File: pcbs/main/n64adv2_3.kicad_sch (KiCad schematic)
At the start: 27 parts, among them U12 TLV70218DBVT, U13 TLV70033

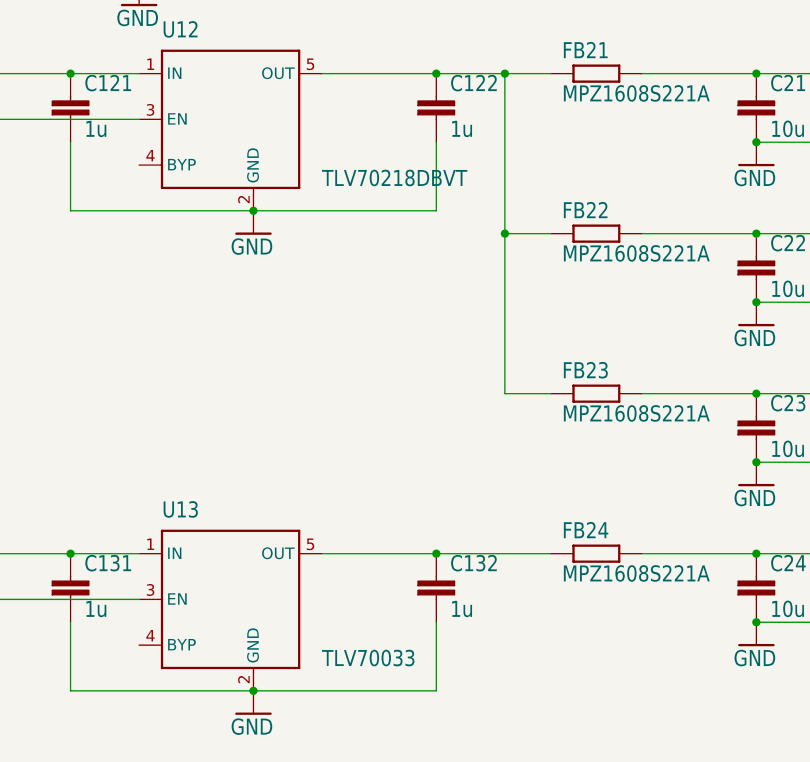
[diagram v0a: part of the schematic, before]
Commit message: update main PCB with minor changes, e.g. ensure that solder mask bridges between 0.5mm pitched pads has min. 0.1mm thickness
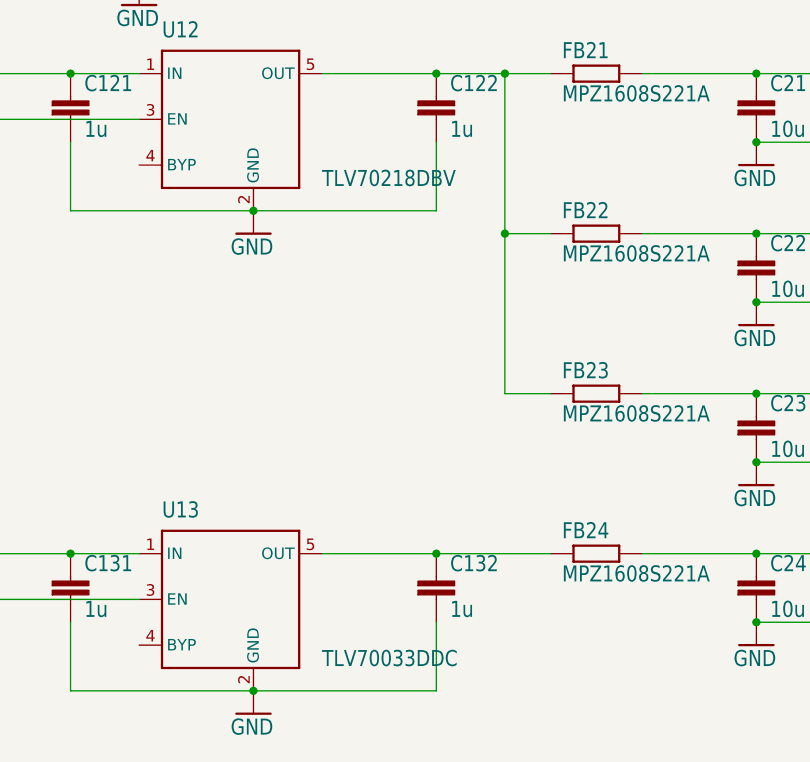
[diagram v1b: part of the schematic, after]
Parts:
- P_5V_IN0, P_GND_2: value (none) -> SMD2; footprint (none) -> n64adv2:SMD1,27-2,54
- U12: value TLV70218DBVT -> TLV70218DBV
- U13: value TLV70033 -> TLV70033DDC
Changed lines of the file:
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@@
       (effects (font (size 1.778 1.5113)) (justify left bottom))
     )
-    (property "Value" "" (id 1) (at 65.278 57.277 0)
+    (property "Value" "SMD2" (id 1) (at 65.278 57.277 0)
       (effects (font (size 1.778 1.5113)) (justify left bottom) hide)
     )
-    (property "Footprint" "" (id 2) (at 68.58 58.42 0)
+    (property "Footprint" "n64adv2:SMD1,27-2,54" (id 2) (at 68.58 58.42 0)
       (effects (font (size 1.27 1.27)) hide)
     )
@@
       (effects (font (size 1.778 1.5113)) (justify left bottom))
     )
-    (property "Value" "TLV70218DBVT" (id 1) (at 127 96.52 0)
+    (property "Value" "TLV70218DBV" (id 1) (at 127 96.52 0)
       (effects (font (size 1.778 1.5113)) (justify left bottom))
     )
@@
       (effects (font (size 1.778 1.5113)) (justify left bottom))
     )
-    (property "Value" "" (id 1) (at 71.882 74.803 0)
+    (property "Value" "SMD2" (id 1) (at 71.882 74.803 0)
       (effects (font (size 1.778 1.5113)) (justify left bottom) hide)
     )
-    (property "Footprint" "" (id 2) (at 68.58 73.66 0)
+    (property "Footprint" "n64adv2:SMD1,27-2,54" (id 2) (at 68.58 73.66 0)
       (effects (font (size 1.27 1.27)) hide)
     )
@@
       (effects (font (size 1.778 1.5113)) (justify left bottom))
     )
-    (property "Value" "TLV70033" (id 1) (at 127 149.86 0)
-      (effects (font (size 1.778 1.5113)) (justify left bottom))
-    )
+    (property "Value" "TLV70033DDC" (id 1) (at 127 149.86 0)
+      (effects (font (size 1.778 1.5113)) (justify left bottom))
+    )

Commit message: update main PCB: - optimize some trace routing - optimize component selection/placing (e.g. HDMI port full SMD, JTAG as SMD alternative) - add license to silkscreen
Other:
- company: (none) -> Peter 'borti4938' Bartmann
- title: (none) -> N64Adv2 (ADV7513)
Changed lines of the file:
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@@
 (kicad_sch (version 20211123) (generator eeschema)
   (paper "A4")
+  (title_block
+    (title "N64Adv2 (ADV7513)")
+    (rev "v20220729")
+    (company "Peter 'borti4938' Bartmann")
+    (comment 1 "Schematic and PCB (c) 2021, 2022 by Peter Bartmann")
+    (comment 2 "N64Adv2_20220729")
+    (comment 3 "Licensed under CERN-OHL-W v2")
+  )
   (junction (at 106.68 71.12) (diameter 0) (color 0 0 0 0)
   )

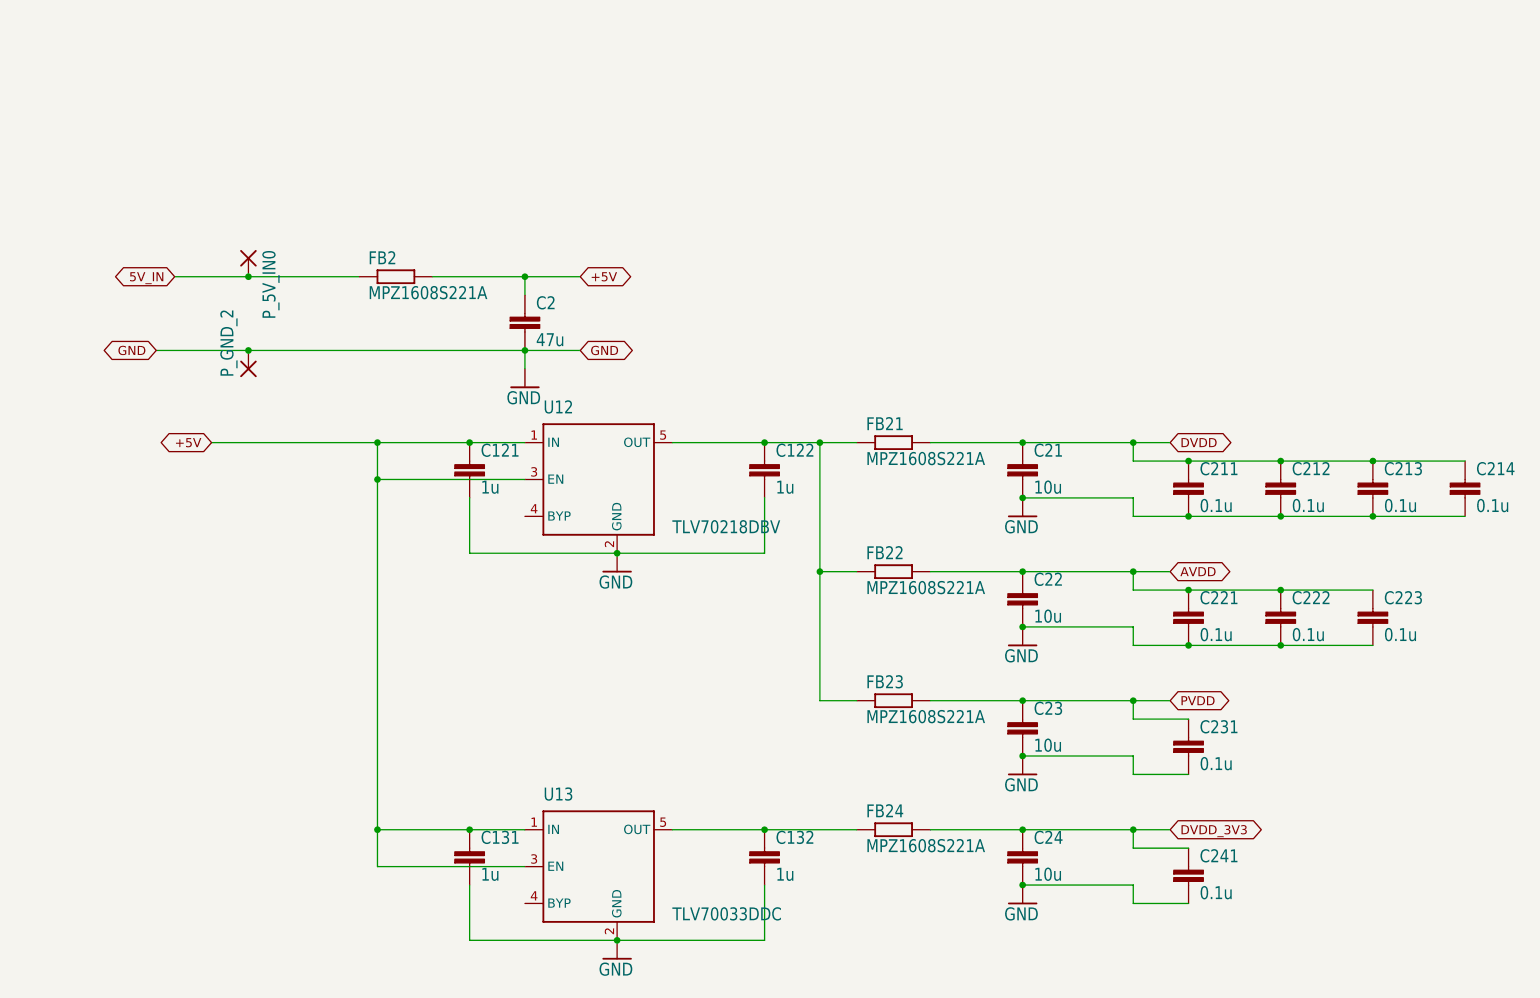
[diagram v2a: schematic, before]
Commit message: update main-pcb: - remove jumper which were left overs from prototype stages - remove some test points - add pads for SPDIF near DIY-IO-Pad area
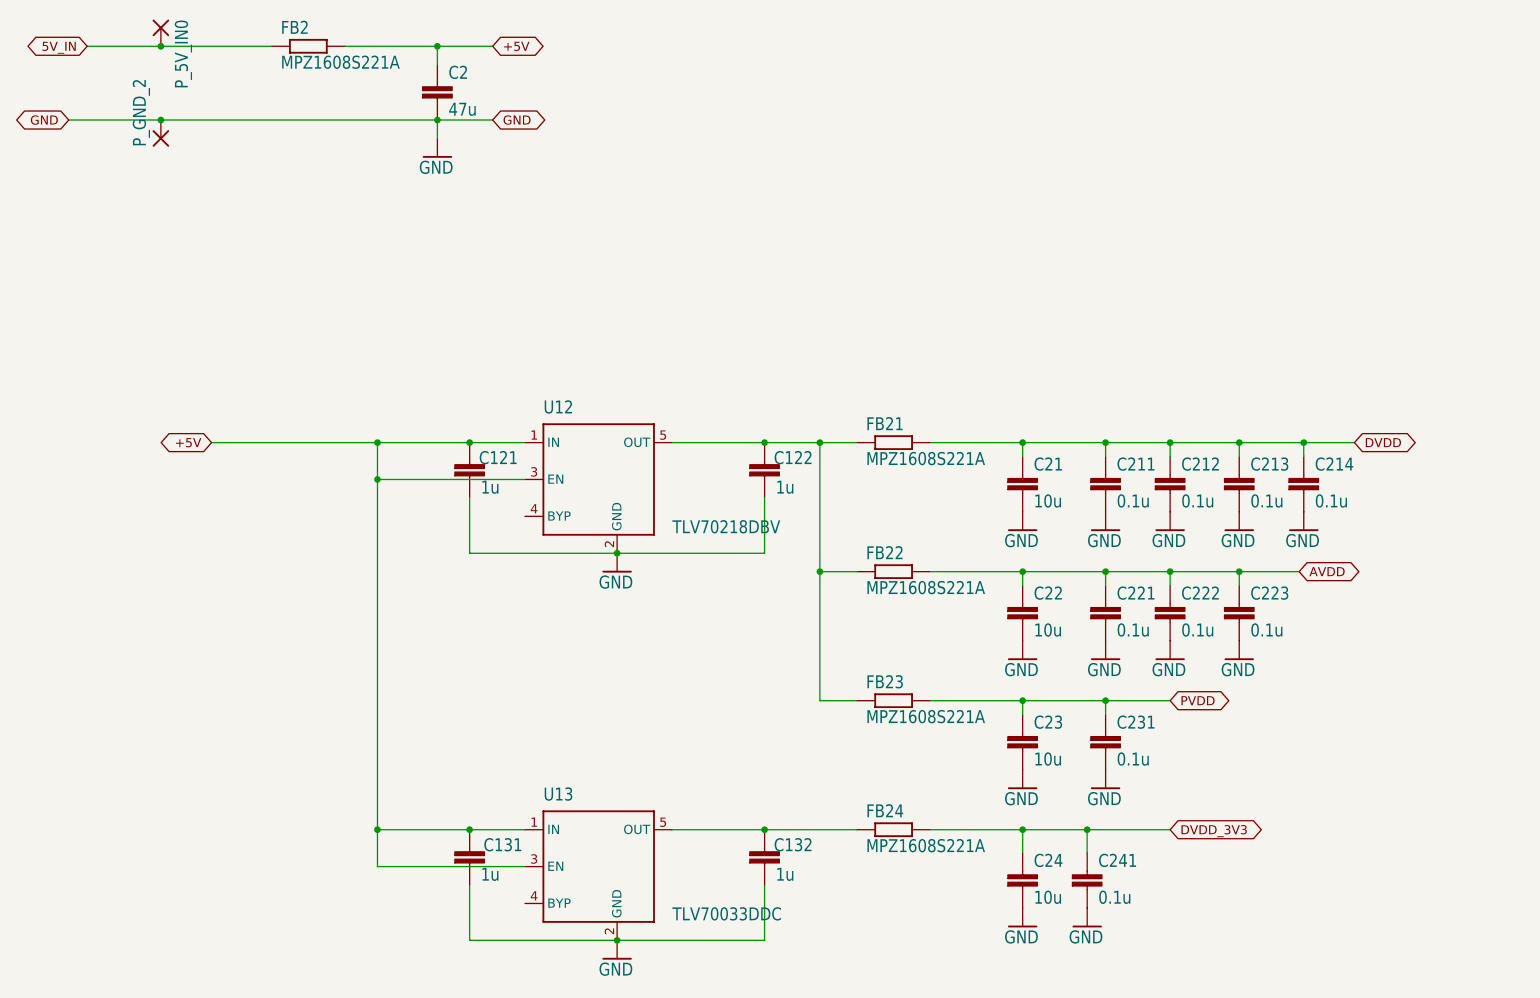
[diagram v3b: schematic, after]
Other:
- title: N64Adv2 (ADV7513) -> N64Adv2
- moved on the sheet: C2, C21, C211, C212, C213, C214, C22, C221, C222, C223, C23, C231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
